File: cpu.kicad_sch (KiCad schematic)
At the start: 36 parts, among them IC901 HUC6280, IC906 LC3664BML-10, Q901 L6

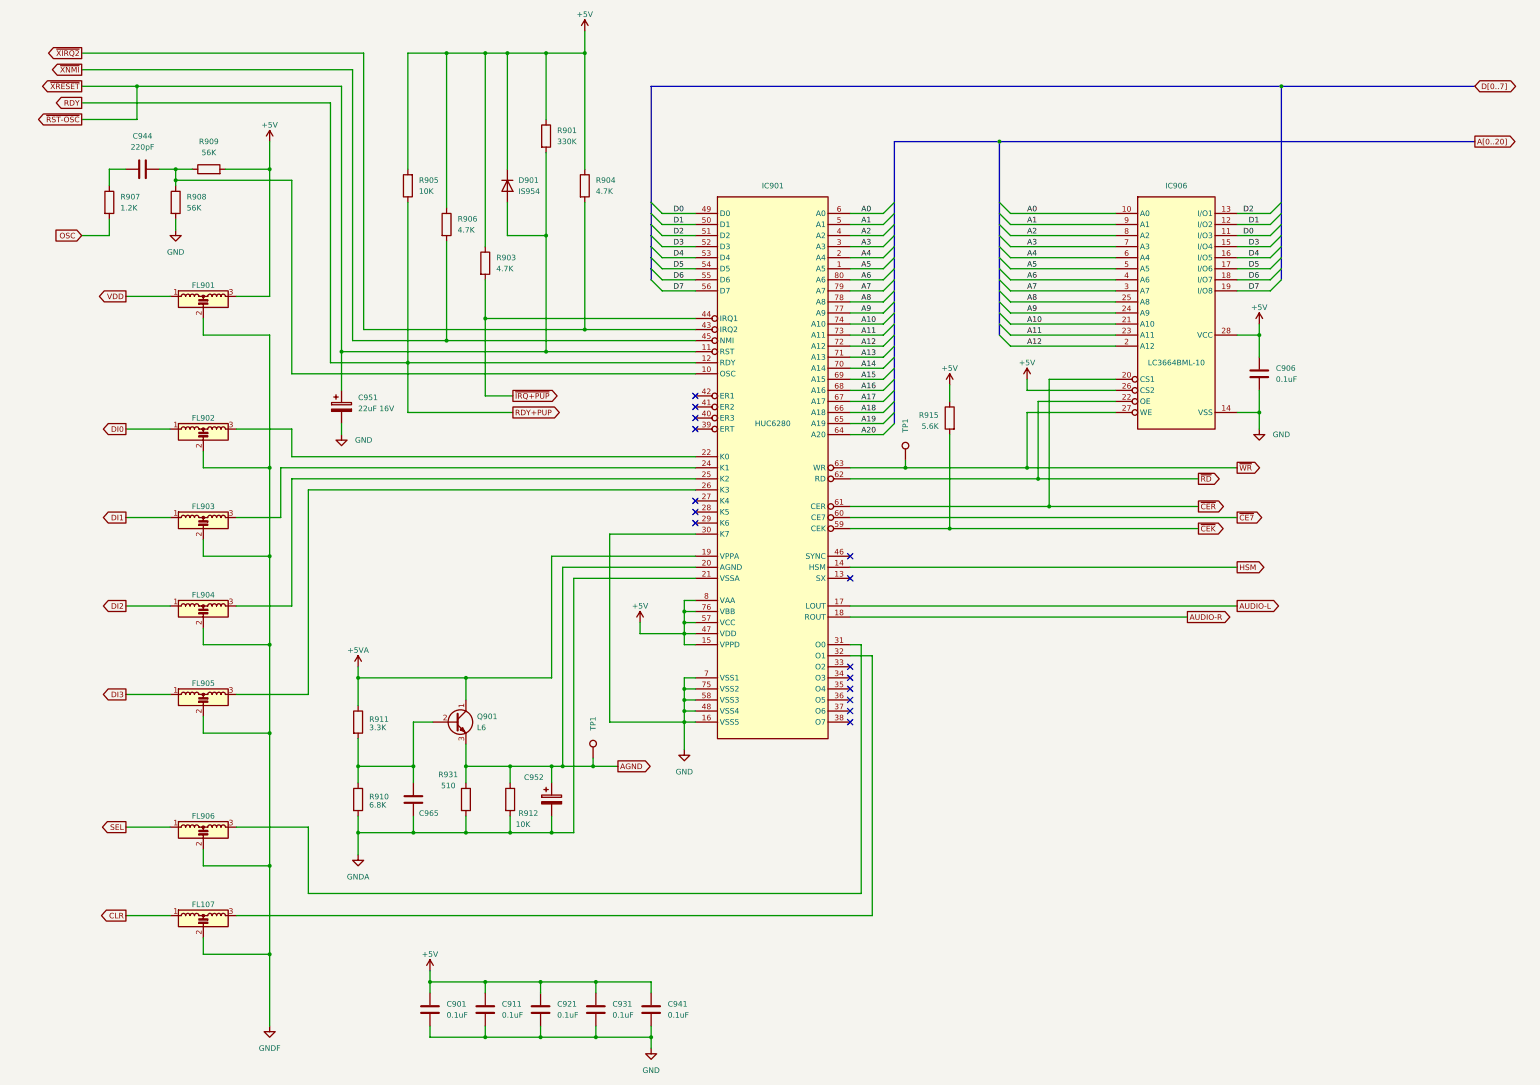
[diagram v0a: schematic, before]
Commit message: Add known capacitor values to schematic. PCB changes: - Corrected C332 -> C322 - Corrected C929 -> C962 - Added missing C166 (extra decoupling for IC105)
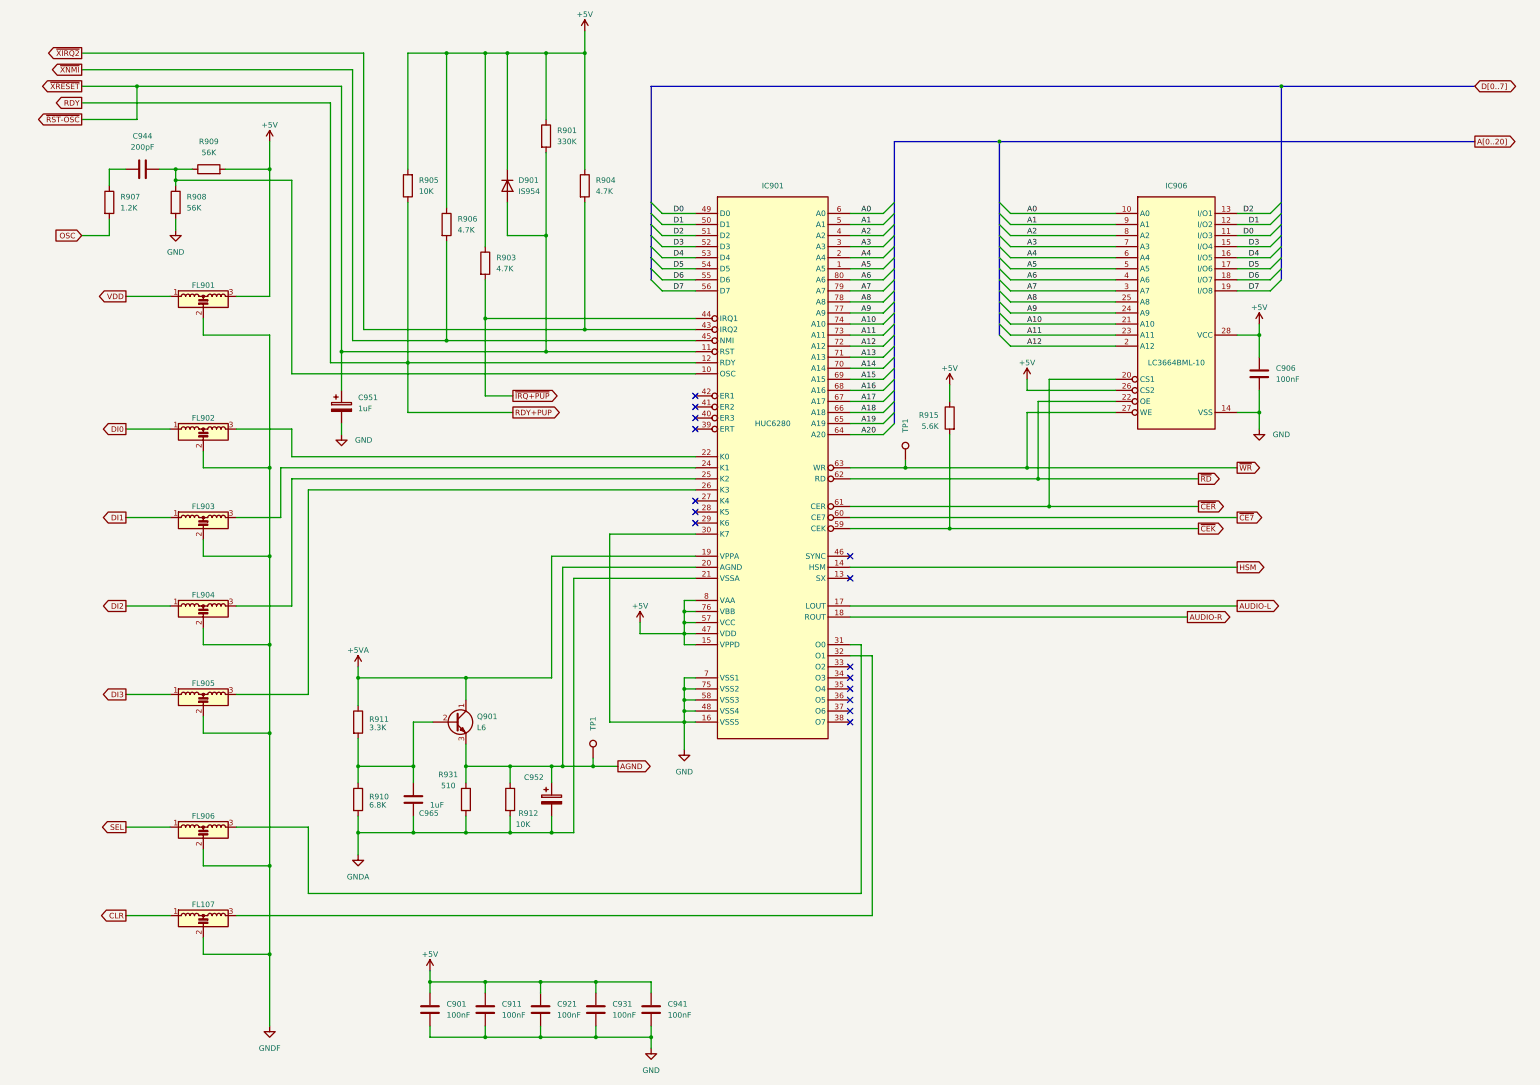
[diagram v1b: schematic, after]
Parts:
- C901, C906, C911, C921, C931, C941: value 0.1uF -> 100nF
- C944: value 220pF -> 200pF
- C951: value 22uF 16V -> 1uF
- C965: value ~ -> 1uF
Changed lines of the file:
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@@
       (effects (font (size 1.27 1.27)) (justify left))
     )
-    (property "Value" "~" (at 132.08 200.66 0)
+    (property "Value" "1uF" (at 132.08 200.66 0)
       (effects (font (size 1.27 1.27)) (justify left))
     )
@@
       (effects (font (size 1.27 1.27)) (justify left))
     )
-    (property "Value" "0.1uF" (at 135.89 248.92 0)
+    (property "Value" "100nF" (at 135.89 248.92 0)
       (effects (font (size 1.27 1.27)) (justify left))
     )
@@
       (effects (font (size 1.27 1.27)) (justify left))
     )
-    (property "Value" "0.1uF" (at 326.39 102.87 0)
+    (property "Value" "100nF" (at 326.39 102.87 0)
       (effects (font (size 1.27 1.27)) (justify left))
     )
@@
       (effects (font (size 1.27 1.27)) (justify left))
     )
-    (property "Value" "0.1uF" (at 161.29 248.92 0)
+    (property "Value" "100nF" (at 161.29 248.92 0)
       (effects (font (size 1.27 1.27)) (justify left))
     )
@@
       (effects (font (size 1.27 1.27)) (justify left))
     )
-    (property "Value" "0.1uF" (at 173.99 248.92 0)
+    (property "Value" "100nF" (at 173.99 248.92 0)
       (effects (font (size 1.27 1.27)) (justify left))
     )
@@
       (effects (font (size 1.27 1.27)))
     )
-    (property "Value" "220pF" (at 66.04 49.53 90)
+    (property "Value" "200pF" (at 66.04 49.53 90)
       (effects (font (size 1.27 1.27)))
     )
@@
       (effects (font (size 1.27 1.27)) (justify left))
     )
-    (property "Value" "22uF 16V" (at 115.57 109.601 0)
+    (property "Value" "1uF" (at 115.57 109.601 0)
       (effects (font (size 1.27 1.27)) (justify left))
     )
@@
       (effects (font (size 1.27 1.27)) (justify left))
     )
-    (property "Value" "0.1uF" (at 186.69 248.92 0)
+    (property "Value" "100nF" (at 186.69 248.92 0)
       (effects (font (size 1.27 1.27)) (justify left))
     )
@@
       (effects (font (size 1.27 1.27)) (justify left))
     )
-    (property "Value" "0.1uF" (at 148.59 248.92 0)
-      (effects (font (size 1.27 1.27)) (justify left))
-    )
+    (property "Value" "100nF" (at 148.59 248.92 0)
+      (effects (font (size 1.27 1.27)) (justify left))
+    )
